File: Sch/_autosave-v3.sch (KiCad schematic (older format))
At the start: 1 part, among them U1 Teensy4.0

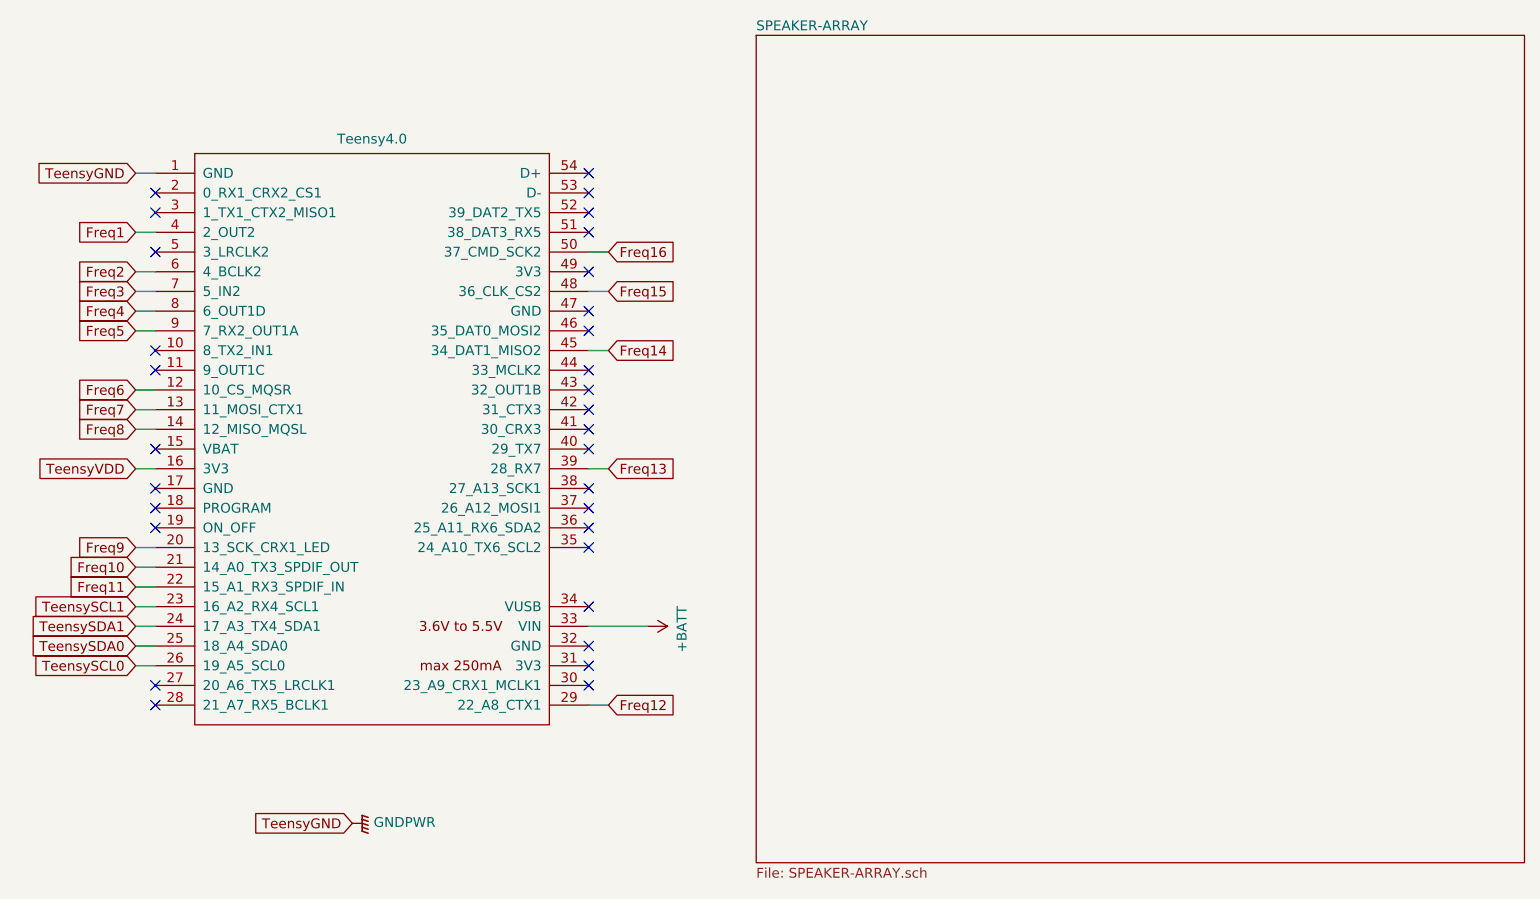
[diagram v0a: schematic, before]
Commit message: Update SCH to include hierachical pages and remove most ERC errors
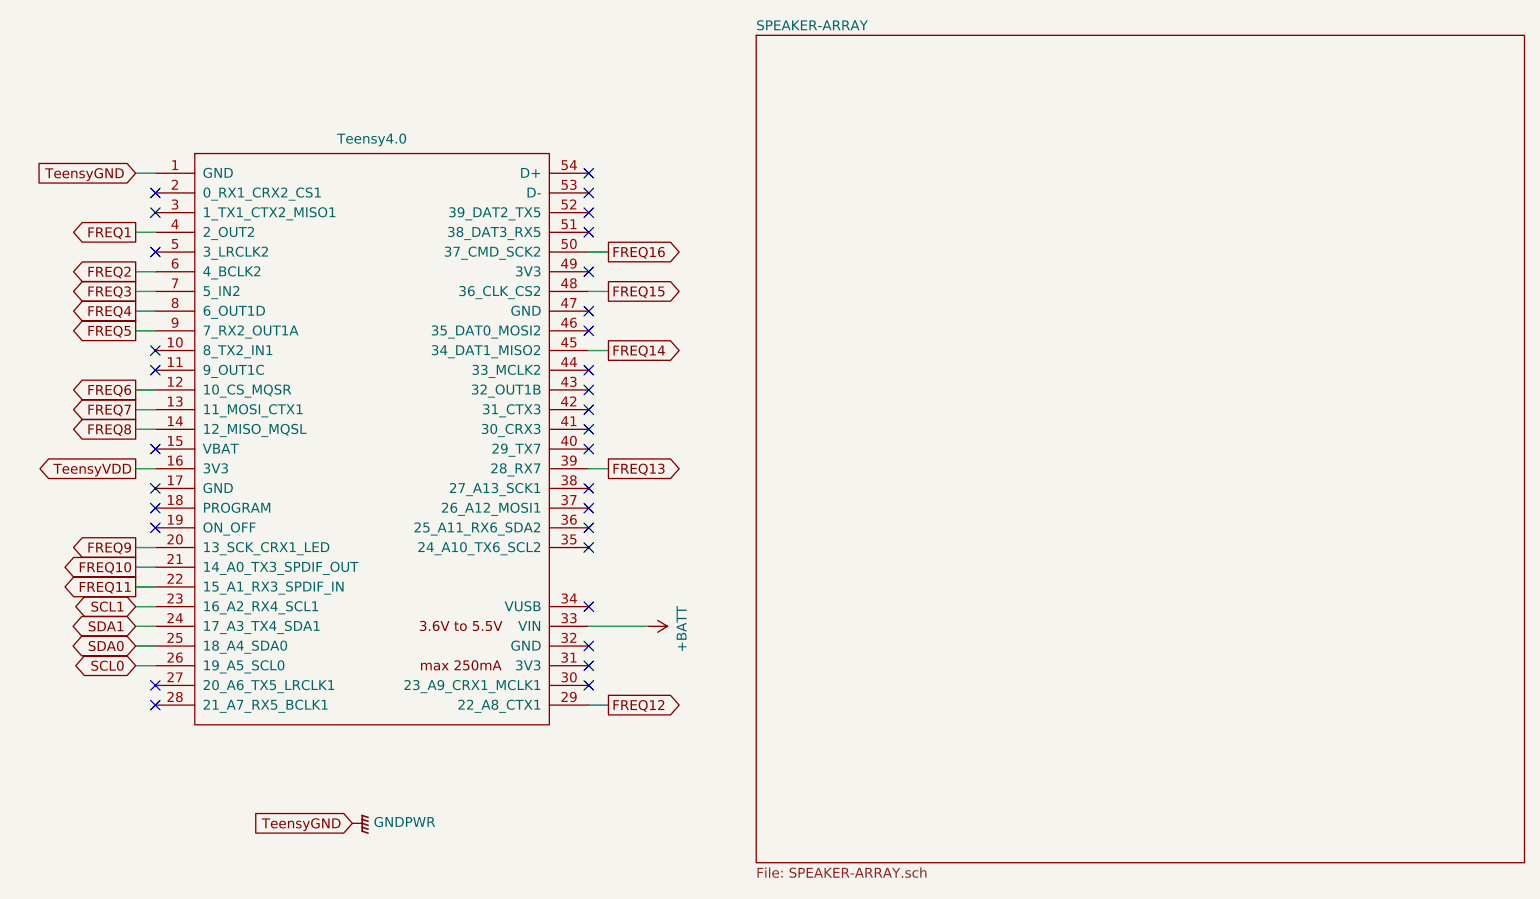
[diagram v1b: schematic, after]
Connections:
- net Freq1 renamed FREQ1
- net Freq10 renamed FREQ10
- net Freq11 renamed FREQ11
- net Freq12 renamed FREQ12
- net Freq13 renamed FREQ13
- net Freq14 renamed FREQ14
- net Freq15 renamed FREQ15
- net Freq16 renamed FREQ16
- net Freq2 renamed FREQ2
- net Freq3 renamed FREQ3
- net Freq4 renamed FREQ4
- net Freq5 renamed FREQ5
- net Freq6 renamed FREQ6
- net Freq7 renamed FREQ7
- net Freq8 renamed FREQ8
- net Freq9 renamed FREQ9
- net TeensySCL0 renamed SCL0
- net TeensySCL1 renamed SCL1
- net TeensySDA0 renamed SDA0
- net TeensySDA1 renamed SDA1
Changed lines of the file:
@@
 Text GLabel 3800 2350 0    50   Input ~ 0
 TeensyGND
-Text GLabel 3800 3850 0    50   Input ~ 0
-TeensyVDD
-Text GLabel 3800 4750 0    50   Input ~ 0
-TeensySDA0
-Text GLabel 3800 4850 0    50   Input ~ 0
-TeensySCL0
 Text GLabel 4900 5650 0    50   Input ~ 0
 TeensyGND
@@
 	0    -1   -1   0
 $EndComp
-Text GLabel 3800 4550 0    50   Input ~ 0
-TeensySCL1
-Text GLabel 3800 4650 0    50   Input ~ 0
-TeensySDA1
-Text GLabel 3800 2650 0    50   Input ~ 0
-Freq1
-Text GLabel 3800 2850 0    50   Input ~ 0
-Freq2
-Text GLabel 3800 2950 0    50   Input ~ 0
-Freq3
-Text GLabel 3800 3050 0    50   Input ~ 0
-Freq4
-Text GLabel 3800 3150 0    50   Input ~ 0
-Freq5
-Text GLabel 3800 3450 0    50   Input ~ 0
-Freq6
-Text GLabel 3800 3550 0    50   Input ~ 0
-Freq7
-Text GLabel 3800 3650 0    50   Input ~ 0
-Freq8
-Text GLabel 3800 4250 0    50   Input ~ 0
-Freq9
-Text GLabel 3800 4350 0    50   Input ~ 0
-Freq10
-Text GLabel 3800 4450 0    50   Input ~ 0
-Freq11
-Text GLabel 6200 5050 2    50   Input ~ 0
-Freq12
-Text GLabel 6200 3850 2    50   Input ~ 0
-Freq13
-Text GLabel 6200 3250 2    50   Input ~ 0
-Freq14
-Text GLabel 6200 2950 2    50   Input ~ 0
-Freq15
-Text GLabel 6200 2750 2    50   Input ~ 0
-Freq16
 Wire Wire Line
 	3800 2350 3900 2350
@@
 NoConn ~ 3900 3750
 NoConn ~ 3900 2750
+Text GLabel 3800 2650 0    50   Output ~ 0
+FREQ1
+Text GLabel 3800 2850 0    50   Output ~ 0
+FREQ2
+Text GLabel 3800 2950 0    50   Output ~ 0
+FREQ3
+Text GLabel 3800 3050 0    50   Output ~ 0
+FREQ4
+Text GLabel 3800 3150 0    50   Output ~ 0
+FREQ5
+Text GLabel 3800 3450 0    50   Output ~ 0
+FREQ6
+Text GLabel 3800 3550 0    50   Output ~ 0
+FREQ7
+Text GLabel 3800 3650 0    50   Output ~ 0
+FREQ8
+Text GLabel 3800 3850 0    50   Output ~ 0
+TeensyVDD
+Text GLabel 3800 4250 0    50   Output ~ 0
+FREQ9
+Text GLabel 3800 4350 0    50   Output ~ 0
+FREQ10
+Text GLabel 3800 4450 0    50   Output ~ 0
+FREQ11
+Text GLabel 3800 4550 0    50   BiDi ~ 0
+SCL1
+Text GLabel 3800 4650 0    50   BiDi ~ 0
+SDA1
+Text GLabel 3800 4750 0    50   BiDi ~ 0
+SDA0
+Text GLabel 3800 4850 0    50   BiDi ~ 0
+SCL0
+Text GLabel 6200 2750 2    50   Output ~ 0
+FREQ16
+Text GLabel 6200 2950 2    50   Output ~ 0
+FREQ15
+Text GLabel 6200 3250 2    50   Output ~ 0
+FREQ14
+Text GLabel 6200 3850 2    50   Output ~ 0
+FREQ13
+Text GLabel 6200 5050 2    50   Output ~ 0
+FREQ12
 $EndSCHEMATC
